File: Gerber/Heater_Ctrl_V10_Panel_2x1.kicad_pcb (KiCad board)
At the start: 2 copper layers, 100 x 100 mm, 82 parts, among them K1 SRD-05VDC-SL-C, K2 SRD-05VDC-SL-C, P1 PWR, P2 DISPLAY, P3 IR_REC, P4 IIC_EXT, P5 Mains, P6 Touch, P7 TH1, P8 TH2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

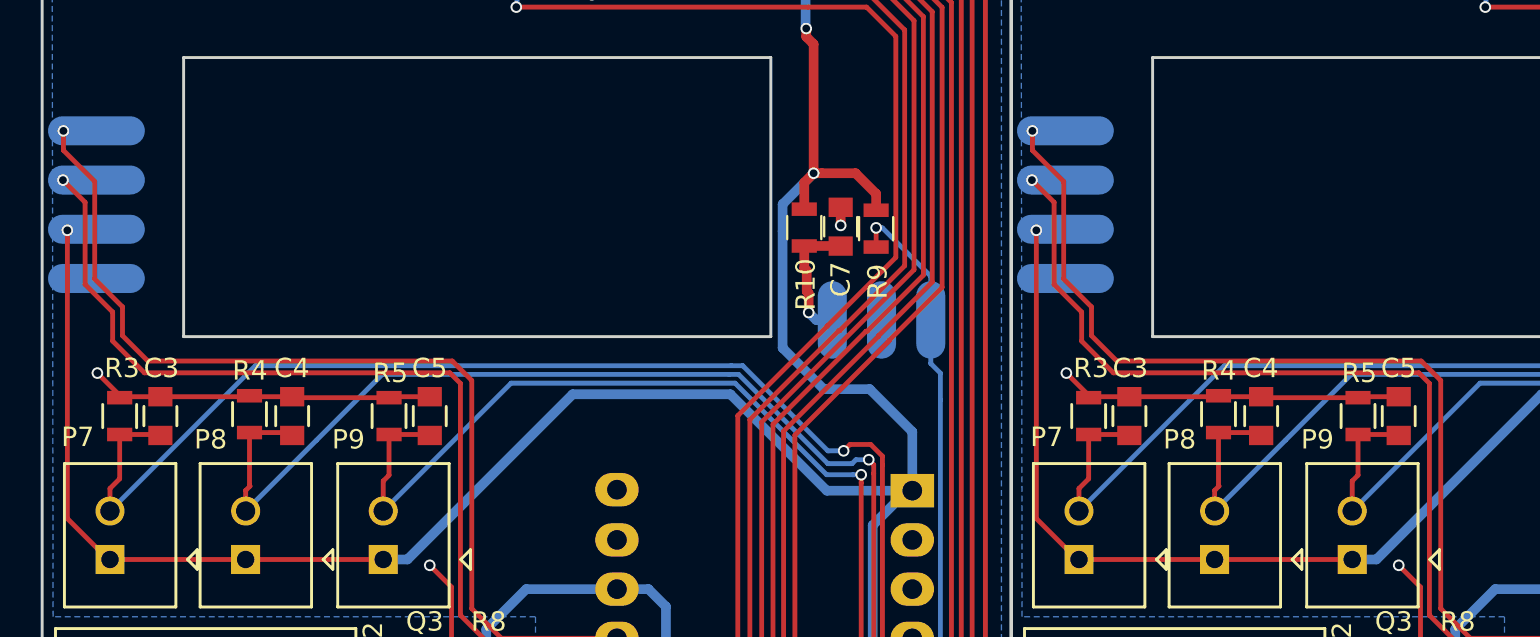
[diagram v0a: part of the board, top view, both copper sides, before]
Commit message: Display Change to TH
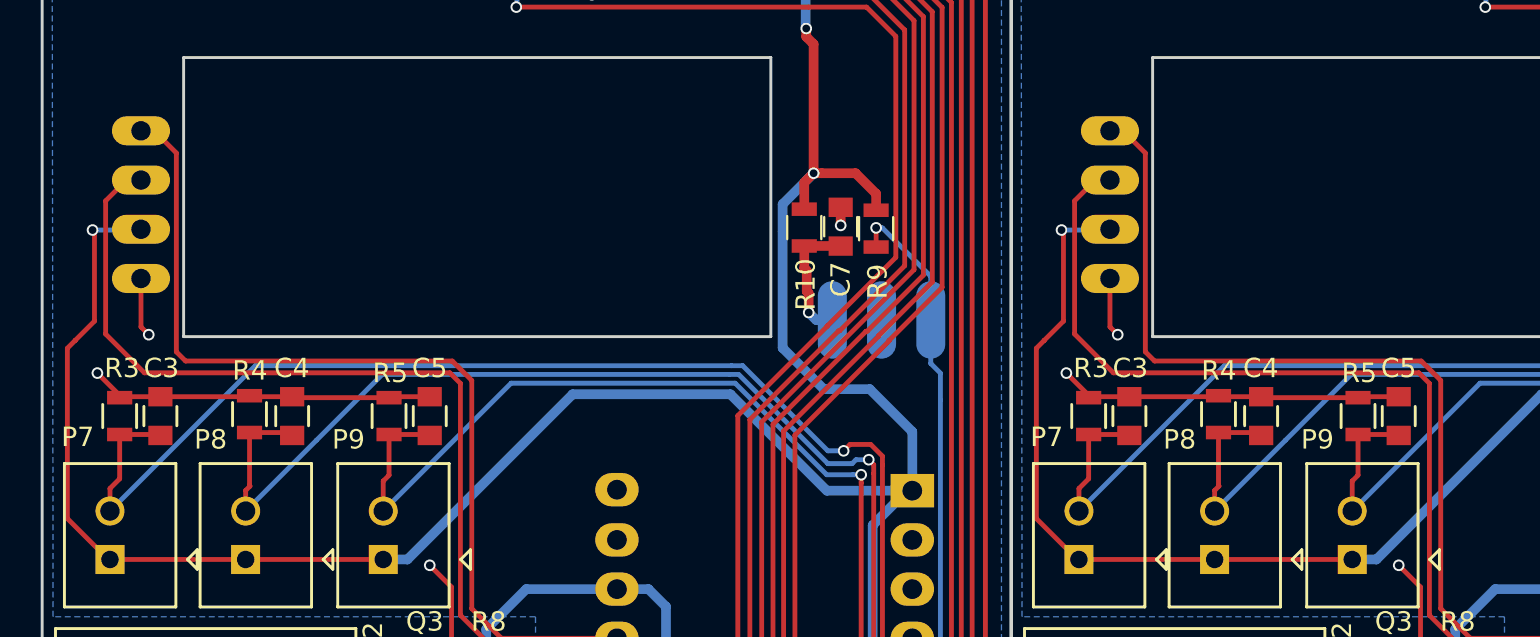
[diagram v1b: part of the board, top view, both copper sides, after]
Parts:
- P2 (x2): footprint Heater_Ctrl:TM1637_Catalex -> Heater_Ctrl:TM1637_Catalex_TH
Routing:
- net /D_CLK: track 104.8 -> 96.6 mm, vias 2 -> 0
- net /D_DIO: track 106.5 -> 100.2 mm, vias 2 -> 0
- net GND: track 97.2 -> 103.4 mm, vias 8 -> 10
